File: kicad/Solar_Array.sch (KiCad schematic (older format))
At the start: 23 parts

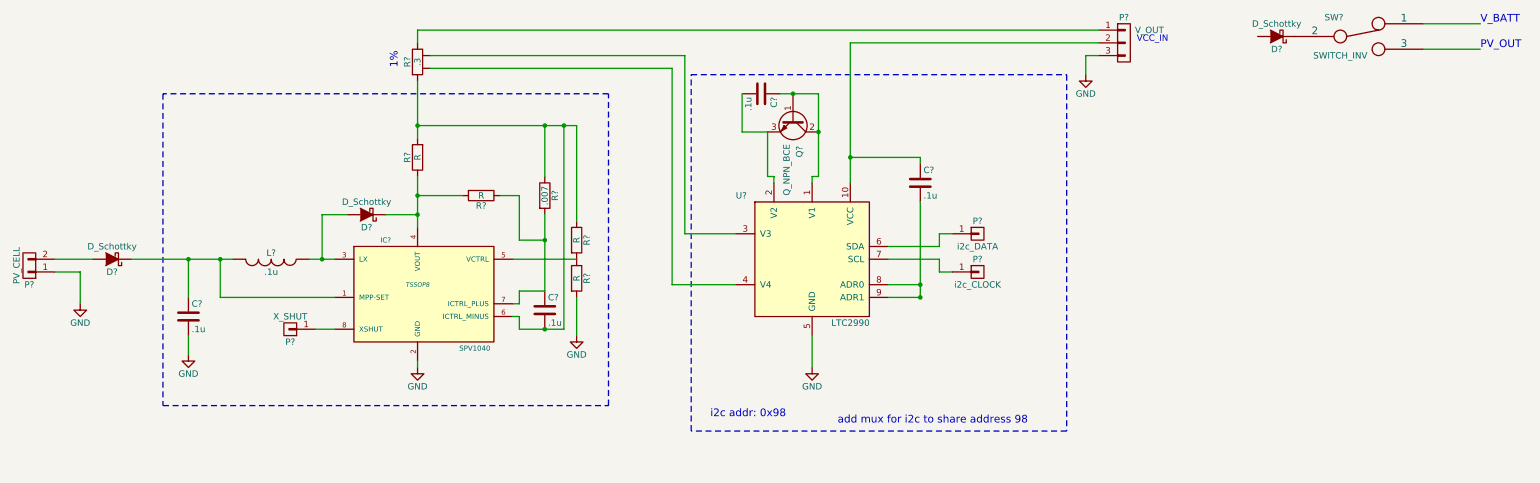
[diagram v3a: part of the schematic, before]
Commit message: Generated Netlist, blocked all I/O to 1x6 pin array.
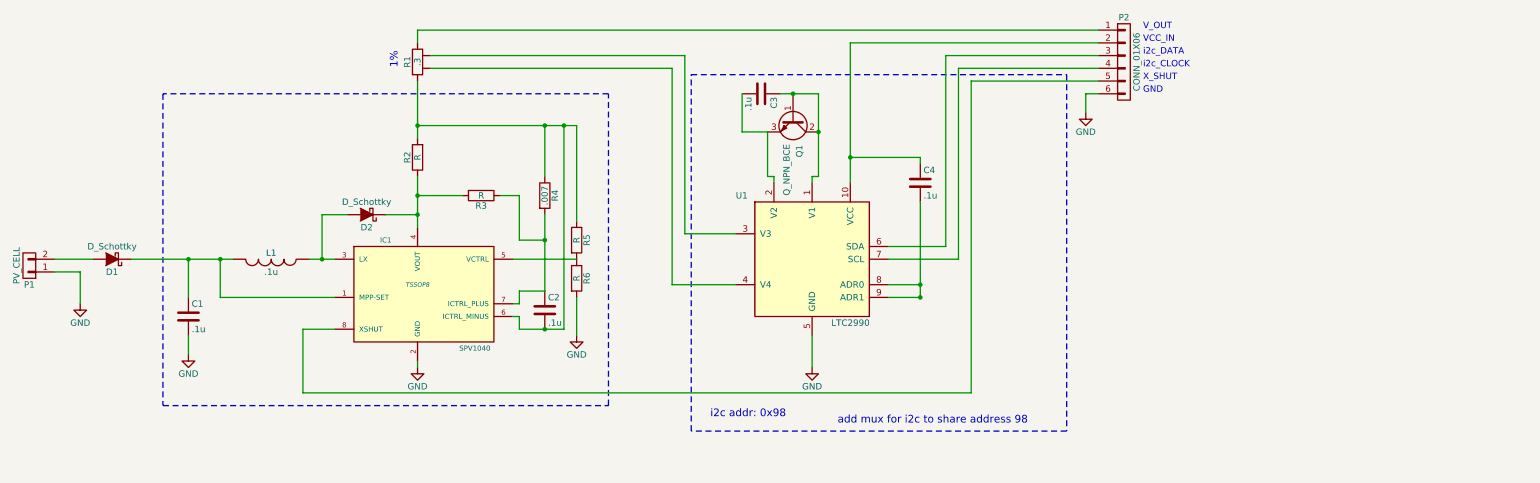
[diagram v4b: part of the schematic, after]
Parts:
- removed D?: D_Schottky, symbol D_Schottky
- removed P?: i2c_CLOCK, symbol CONN_01X01
- removed P?: i2c_DATA, symbol CONN_01X01
- removed P?: X_SHUT, symbol CONN_01X01
- removed P?: V_OUT, symbol CONN_01X03
- removed SW?: SWITCH_INV, symbol SWITCH_INV
- added P2: CONN_01X06, symbol CONN_01X06
- gave numbers to parts that had none: 17
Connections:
- net GND: now also P2.6 (P6)
- net at C4.1, U1.10 (VCC): now also P2.2 (P2)
- net at U1.6 (SDA): now also P2.3 (P3)
- net at U1.7 (SCL): now also P2.4 (P4)
- net at R1.1: now also P2.1 (P1)
- net at IC1.8 (XSHUT): now also P2.5 (P5)
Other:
- note added: "GND"
- note added: "V_OUT"
- note added: "X_SHUT"
- note added: "i2c_CLOCK"
- note added: "i2c_DATA"
- note removed: "PV_OUT"
- note removed: "V_BATT"
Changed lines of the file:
@@
 LIBS:contrib
 LIBS:valves
-LIBS:Launch_Tower_Computer_III-cache
 LIBS:Solar_Array-cache
 EELAYER 25 0
@@
 $EndDescr
 $Comp
-L LTC2990 U?
+L LTC2990 U1
 U 1 1 56A79694
 P 7000 2750
-F 0 "U?" H 6400 3250 50  0000 L CNN
+F 0 "U1" H 6400 3250 50  0000 L CNN
 F 1 "LTC2990" H 7150 2250 50  0000 L CNN
 F 2 "" H 6300 3150 50  0000 C CNN
@@
 $EndComp
 $Comp
-L GND #PWR?
+L GND #PWR01
 U 1 1 56A7969A
 P 7000 3600
-F 0 "#PWR?" H 7000 3350 50  0001 C CNN
+F 0 "#PWR01" H 7000 3350 50  0001 C CNN
 F 1 "GND" H 7000 3450 50  0000 C CNN
 F 2 "" H 7000 3600 60  0000 C CNN
@@
 i2c addr: 0x98
 $Comp
-L R4T R?
+L R4T R1
 U 1 1 56A79735
 P 3900 1200
-F 0 "R?" V 3820 1200 50  0000 C CNN
+F 0 "R1" V 3820 1200 50  0000 C CNN
 F 1 ".3" V 3900 1200 50  0000 C CNN
 F 2 "" V 3830 1200 30  0000 C CNN
@@
 $EndComp
 $Comp
-L Q_NPN_BCE Q?
+L Q_NPN_BCE Q1
 U 1 1 56A7974E
 P 6850 1650
-F 0 "Q?" H 7150 1700 50  0000 R CNN
+F 0 "Q1" H 7150 1700 50  0000 R CNN
 F 1 "Q_NPN_BCE" H 7450 1600 50  0000 R CNN
 F 2 "" H 7050 1750 29  0000 C CNN
@@
 $EndComp
 $Comp
-L C C?
+L C C3
 U 1 1 56A7975A
 P 6600 1450
-F 0 "C?" H 6625 1550 50  0000 L CNN
+F 0 "C3" H 6625 1550 50  0000 L CNN
 F 1 ".1u" H 6625 1350 50  0000 L CNN
 F 2 "" H 6638 1300 30  0000 C CNN
@@
 $EndComp
 $Comp
-L C C?
+L C C4
 U 1 1 56A7DA5A
 P 7850 2150
-F 0 "C?" H 7875 2250 50  0000 L CNN
+F 0 "C4" H 7875 2250 50  0000 L CNN
 F 1 ".1u" H 7875 2050 50  0000 L CNN
 F 2 "" H 7888 2000 30  0000 C CNN
@@
 add mux for i2c to share address 98
 $Comp
-L GND #PWR?
+L GND #PWR02
 U 1 1 56A96BD7
 P 1250 3100
-F 0 "#PWR?" H 1250 2850 50  0001 C CNN
+F 0 "#PWR02" H 1250 2850 50  0001 C CNN
 F 1 "GND" H 1250 2950 50  0000 C CNN
 F 2 "" H 1250 3100 60  0000 C CNN
@@
 $EndComp
 $Comp
-L SPV1040 IC?
+L SPV1040 IC1
 U 1 1 56A9734E
 P 3950 3000
-F 0 "IC?" H 3650 3400 40  0000 C CNN
+F 0 "IC1" H 3650 3400 40  0000 C CNN
 F 1 "SPV1040" H 4350 2550 40  0000 C CNN
 F 2 "TSSOP8" H 3900 3050 35  0000 C CIN
@@
 $EndComp
 $Comp
-L INDUCTOR L?
+L INDUCTOR L1
 U 1 1 56A973BB
 P 2750 2750
-F 0 "L?" V 2700 2750 50  0000 C CNN
+F 0 "L1" V 2700 2750 50  0000 C CNN
 F 1 ".1u" V 2850 2750 50  0000 C CNN
 F 2 "" H 2750 2750 60  0000 C CNN
@@
 $EndComp
 $Comp
-L C C?
+L C C1
 U 1 1 56A97517
 P 2100 3200
-F 0 "C?" H 2125 3300 50  0000 L CNN
+F 0 "C1" H 2125 3300 50  0000 L CNN
 F 1 ".1u" H 2125 3100 50  0000 L CNN
 F 2 "" H 2138 3050 30  0000 C CNN
@@
 $EndComp
 $Comp
-L GND #PWR?
+L GND #PWR03
 U 1 1 56A97606
 P 2100 3500
-F 0 "#PWR?" H 2100 3250 50  0001 C CNN
+F 0 "#PWR03" H 2100 3250 50  0001 C CNN
 F 1 "GND" H 2100 3350 50  0000 C CNN
 F 2 "" H 2100 3500 60  0000 C CNN
@@
 $EndComp
 $Comp
-L C C?
+L C C2
 U 1 1 56A9778A
 P 4900 3150
-F 0 "C?" H 4925 3250 50  0000 L CNN
+F 0 "C2" H 4925 3250 50  0000 L CNN
 F 1 ".1u" H 4925 3050 50  0000 L CNN
 F 2 "" H 4938 3000 30  0000 C CNN
@@
 $EndComp
 $Comp
-L R R?
+L R R5
 U 1 1 56A97A23
 P 5150 2600
-F 0 "R?" V 5230 2600 50  0000 C CNN
+F 0 "R5" V 5230 2600 50  0000 C CNN
 F 1 "R" V 5150 2600 50  0000 C CNN
 F 2 "" V 5080 2600 30  0000 C CNN
@@
 $EndComp
 $Comp
-L R R?
+L R R6
 U 1 1 56A97AAE
 P 5150 2900
-F 0 "R?" V 5230 2900 50  0000 C CNN
+F 0 "R6" V 5230 2900 50  0000 C CNN
 F 1 "R" V 5150 2900 50  0000 C CNN
 F 2 "" V 5080 2900 30  0000 C CNN
@@
 $EndComp
 $Comp
-L GND #PWR?
+L GND #PWR04
 U 1 1 56A97B91
 P 5150 3350
-F 0 "#PWR?" H 5150 3100 50  0001 C CNN
+F 0 "#PWR04" H 5150 3100 50  0001 C CNN
 F 1 "GND" H 5150 3200 50  0000 C CNN
 F 2 "" H 5150 3350 60  0000 C CNN
@@
 $EndComp
 $Comp
-L D_Schottky D?
+L D_Schottky D2
 U 1 1 56A97CB5
 P 3500 2400
-F 0 "D?" H 3500 2500 50  0000 C CNN
+F 0 "D2" H 3500 2500 50  0000 C CNN
 F 1 "D_Schottky" H 3500 2300 50  0000 C CNN
 F 2 "" H 3500 2400 60  0000 C CNN
@@
 $EndComp
 $Comp
-L R R?
+L R R3
 U 1 1 56A9803B
 P 4400 2250
-F 0 "R?" V 4480 2250 50  0000 C CNN
+F 0 "R3" V 4480 2250 50  0000 C CNN
 F 1 "R" V 4400 2250 50  0000 C CNN
 F 2 "" V 4330 2250 30  0000 C CNN
@@
 $EndComp
 $Comp
-L R R?
+L R R2
 U 1 1 56A981E3
 P 3900 1950
-F 0 "R?" V 3980 1950 50  0000 C CNN
+F 0 "R2" V 3980 1950 50  0000 C CNN
 F 1 "R" V 3900 1950 50  0000 C CNN
 F 2 "" V 3830 1950 30  0000 C CNN
@@
 $EndComp
 $Comp
-L R R?
+L R R4
 U 1 1 56A98B14
 P 4900 2250
-F 0 "R?" V 4980 2250 50  0000 C CNN
+F 0 "R4" V 4980 2250 50  0000 C CNN
 F 1 ".007" V 4900 2250 50  0000 C CNN
 F 2 "" V 4830 2250 30  0000 C CNN
@@
 $EndComp
 $Comp
-L GND #PWR?
+L GND #PWR05
 U 1 1 56A99359
 P 3900 3600
-F 0 "#PWR?" H 3900 3350 50  0001 C CNN
+F 0 "#PWR05" H 3900 3350 50  0001 C CNN
 F 1 "GND" H 3900 3450 50  0000 C CNN
 F 2 "" H 3900 3600 60  0000 C CNN
@@
 $EndComp
 $Comp
-L CONN_01X01 P?
-U 1 1 56A9AD7A
-P 8300 2850
-F 0 "P?" H 8300 2950 50  0000 C CNN
-F 1 "i2c_CLOCK" H 8300 2750 50  0000 C CNN
-F 2 "" H 8300 2850 60  0000 C CNN
-F 3 "" H 8300 2850 60  0000 C CNN
-	1    8300 2850
-	1    0    0    -1
-$EndComp
-$Comp
-L CONN_01X01 P?
-U 1 1 56A9B08F
-P 8300 2550
-F 0 "P?" H 8300 2650 50  0000 C CNN
-F 1 "i2c_DATA" H 8300 2450 50  0000 C CNN
-F 2 "" H 8300 2550 60  0000 C CNN
-F 3 "" H 8300 2550 60  0000 C CNN
-	1    8300 2550
-	1    0    0    -1
-$EndComp
-$Comp
-L GND #PWR?
+L GND #PWR06
 U 1 1 56A9DF6A
-P 9150 1300
-F 0 "#PWR?" H 9150 1050 50  0001 C CNN
-F 1 "GND" H 9150 1150 50  0000 C CNN
-F 2 "" H 9150 1300 60  0000 C CNN
-F 3 "" H 9150 1300 60  0000 C CNN
-	1    9150 1300
-	1    0    0    -1
-$EndComp
-$Comp
-L CONN_01X02 P?
+P 9150 1600
+F 0 "#PWR06" H 9150 1350 50  0001 C CNN
+F 1 "GND" H 9150 1450 50  0000 C CNN
+F 2 "" H 9150 1600 60  0000 C CNN
+F 3 "" H 9150 1600 60  0000 C CNN
+	1    9150 1600
+	1    0    0    -1
+$EndComp
+$Comp
+L CONN_01X02 P1
 U 1 1 56A9E16B
 P 850 2800
-F 0 "P?" H 850 2950 50  0000 C CNN
+F 0 "P1" H 850 2950 50  0000 C CNN
 F 1 "PV_CELL" V 950 2800 50  0000 C CNN
 F 2 "" H 850 2800 60  0000 C CNN
@@
 	-1   0    0    1
 $EndComp
-$Comp
-L CONN_01X01 P?
-U 1 1 56AA3494
-P 2900 3300
-F 0 "P?" H 2900 3400 50  0000 C CNN
-F 1 "X_SHUT" H 2900 3200 50  0000 C CNN
-F 2 "" H 2900 3300 60  0000 C CNN
-F 3 "" H 2900 3300 60  0000 C CNN
-	1    2900 3300
-	-1   0    0    1
-$EndComp
-$Comp
-L CONN_01X03 P?
-U 1 1 56AA5ABE
-P 9450 1050
-F 0 "P?" H 9450 1250 50  0000 C CNN
-F 1 "V_OUT" H 9650 1150 50  0000 C CNN
-F 2 "" H 9450 1050 60  0000 C CNN
-F 3 "" H 9450 1050 60  0000 C CNN
-	1    9450 1050
-	1    0    0    -1
-$EndComp
-Text Notes 9550 1050 0    50   ~ 0
+Text Notes 9600 1050 0    50   ~ 0
 VCC_IN
 $Comp
-L D_Schottky D?
+L D_Schottky D1
 U 1 1 56AA70D2
 P 1500 2750
-F 0 "D?" H 1500 2850 50  0000 C CNN
+F 0 "D1" H 1500 2850 50  0000 C CNN
 F 1 "D_Schottky" H 1500 2650 50  0000 C CNN
 F 2 "" H 1500 2750 60  0000 C CNN
@@
 Connection ~ 2100 2750
 Wire Wire Line
-	7600 2750 8000 2750
-Wire Wire Line
-	8000 2750 8000 2850
-Wire Wire Line
-	8000 2850 8100 2850
-Wire Wire Line
-	7600 2650 8000 2650
-Wire Wire Line
-	8000 2650 8000 2550
-Wire Wire Line
-	8000 2550 8100 2550
+	7600 2750 8150 2750
+Wire Wire Line
+	7600 2650 8050 2650
 Wire Wire Line
 	4700 2250 4700 2600
@@
 	3900 950  3900 1050
 Wire Wire Line
-	3100 3300 3250 3300
+	3000 3300 3250 3300
 Wire Wire Line
 	3900 1700 5150 1700
@@
 	3900 2250 4250 2250
 Wire Wire Line
-	9150 1150 9250 1150
-Wire Wire Line
-	9150 1150 9150 1300
+	8050 1150 9250 1150
 Wire Wire Line
 	7300 1050 9250 1050
@@
 Wire Wire Line
 	1650 2750 2450 2750
-$Comp
-L D_Schottky D?
-U 1 1 56AC3033
-P 10650 1000
-F 0 "D?" H 10650 1100 50  0000 C CNN
-F 1 "D_Schottky" H 10650 900 50  0000 C CNN
-F 2 "" H 10650 1000 60  0000 C CNN
-F 3 "" H 10650 1000 60  0000 C CNN
-	1    10650 1000
-	-1   0    0    1
-$EndComp
-$Comp
-L SWITCH_INV SW?
-U 1 1 56AC30B8
-P 11300 1000
-F 0 "SW?" H 11100 1150 50  0000 C CNN
-F 1 "SWITCH_INV" H 11150 850 50  0000 C CNN
-F 2 "" H 11300 1000 60  0000 C CNN
-F 3 "" H 11300 1000 60  0000 C CNN
-	1    11300 1000
-	1    0    0    -1
-$EndComp
-Wire Wire Line
-	11800 900  12250 900
-Wire Wire Line
-	11800 1100 12250 1100
-Text Notes 12250 900  0    60   ~ 0
-V_BATT
-Text Notes 12250 1100 0    60   ~ 0
-PV_OUT
+Wire Wire Line
+	8250 1350 9250 1350
+Wire Wire Line
+	8050 2650 8050 1150
+Wire Wire Line
+	8150 2750 8150 1250
+Wire Wire Line
+	8150 1250 9250 1250
+$Comp
+L CONN_01X06 P2
+U 1 1 56B283C9
+P 9450 1200
+F 0 "P2" H 9450 1550 50  0000 C CNN
+F 1 "CONN_01X06" V 9550 1200 50  0000 C CNN
+F 2 "" H 9450 1200 60  0000 C CNN
+F 3 "" H 9450 1200 60  0000 C CNN
+	1    9450 1200
+	1    0    0    -1
+$EndComp
+Wire Wire Line
+	9250 1450 9150 1450
+Wire Wire Line
+	9150 1450 9150 1600
+Wire Wire Line
+	8250 1350 8250 3800
+Wire Wire Line
+	8250 3800 3000 3800
+Wire Wire Line
+	3000 3800 3000 3300
+Text Notes 9600 950  0    50   ~ 0
+V_OUT
+Text Notes 9600 1150 0    50   ~ 0
+i2c_DATA
+Text Notes 9600 1250 0    50   ~ 0
+i2c_CLOCK
+Text Notes 9600 1350 0    50   ~ 0
+X_SHUT
+Text Notes 9600 1450 0    50   ~ 0
+GND
 $EndSCHEMATC

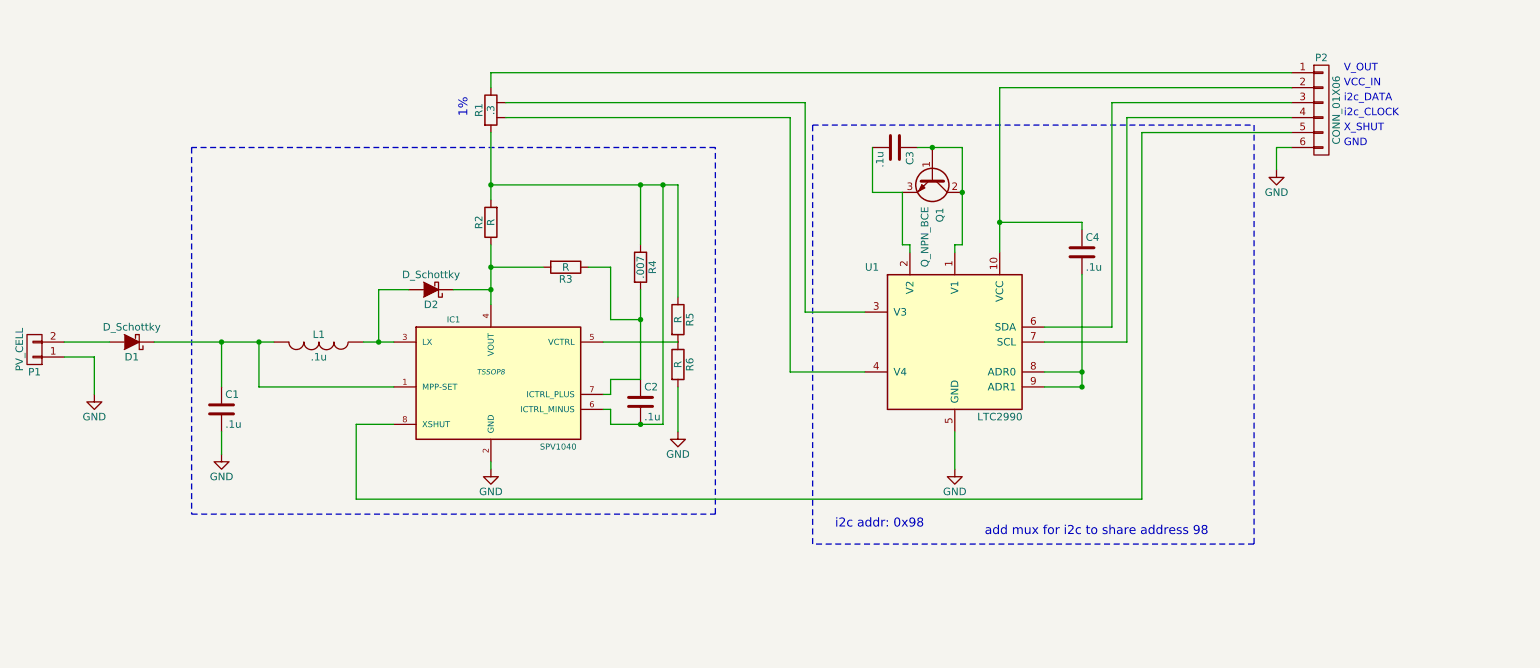
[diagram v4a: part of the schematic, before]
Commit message: Removed input shotkey diode, adde design notes, readdressed ltc2990.
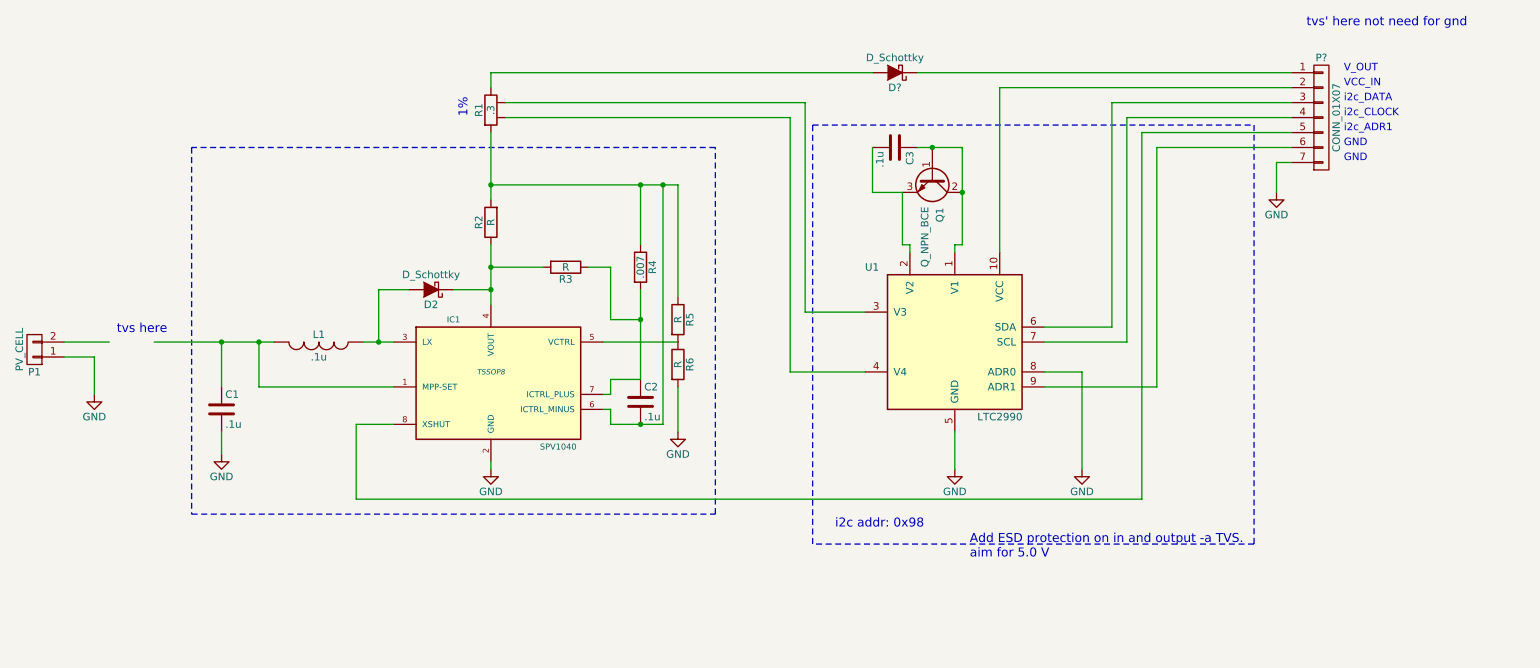
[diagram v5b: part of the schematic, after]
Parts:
- removed C4: .1u, symbol C
- removed D1: D_Schottky, symbol D_Schottky
- removed P2: CONN_01X06, symbol CONN_01X06
- added D?: D_Schottky, symbol D_Schottky
- added P?: CONN_01X07, symbol CONN_01X07
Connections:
- net GND: now also U1.8 (ADR0), P?.7 (P7)
- net at U1.10 (VCC): now also P?.2 (P2)
- net at U1.6 (SDA): now also P?.3 (P3)
- net at U1.7 (SCL): now also P?.4 (P4)
- net at U1.9 (ADR1): now also P?.6 (P6); no longer U1.8 (ADR0)
- net at R1.1: now also D?.2 (A)
- net at IC1.8 (XSHUT): now also P?.5 (P5)
- new net: D?.1 (K), P?.1 (P1)
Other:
- note added: "Add ESD protection on in and output -a TVS.\naim for 5.0 V"
- note added: "i2c_ADR1"
- note added: "tvs here"
- note added: "tvs' here not need for gnd"
- note removed: "X_SHUT"
- note removed: "add mux for i2c to share address 98"
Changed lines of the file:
@@
 LIBS:contrib
 LIBS:valves
+LIBS:Launch_Tower_Computer_III-cache
 LIBS:Solar_Array-cache
 EELAYER 25 0
@@
 	0    1    1    0
 $EndComp
-$Comp
-L C C4
-U 1 1 56A7DA5A
-P 7850 2150
-F 0 "C4" H 7875 2250 50  0000 L CNN
-F 1 ".1u" H 7875 2050 50  0000 L CNN
-F 2 "" H 7888 2000 30  0000 C CNN
-F 3 "" H 7850 2150 60  0000 C CNN
-	1    7850 2150
-	1    0    0    -1
-$EndComp
 Text Notes 1200 9750 0    60   ~ 0
 ToDo:\n***Select component values\n***Design more robust automatic shutdown\n***Add mux for i2c\n***Low voltage warning to payload for save and reboot.\n***3.3v for uC (10 ma each uC)\n***PA need 20V
 Text Notes 3750 1250 1    60   ~ 0
 1%
-Text Notes 7200 4050 0    60   ~ 0
-add mux for i2c to share address 98
 $Comp
 L GND #PWR02
@@
 L GND #PWR06
 U 1 1 56A9DF6A
-P 9150 1600
-F 0 "#PWR06" H 9150 1350 50  0001 C CNN
-F 1 "GND" H 9150 1450 50  0000 C CNN
-F 2 "" H 9150 1600 60  0000 C CNN
-F 3 "" H 9150 1600 60  0000 C CNN
-	1    9150 1600
+P 9150 1750
+F 0 "#PWR06" H 9150 1500 50  0001 C CNN
+F 1 "GND" H 9150 1600 50  0000 C CNN
+F 2 "" H 9150 1750 60  0000 C CNN
+F 3 "" H 9150 1750 60  0000 C CNN
+	1    9150 1750
 	1    0    0    -1
 $EndComp
@@
 Text Notes 9600 1050 0    50   ~ 0
 VCC_IN
-$Comp
-L D_Schottky D1
-U 1 1 56AA70D2
-P 1500 2750
-F 0 "D1" H 1500 2850 50  0000 C CNN
-F 1 "D_Schottky" H 1500 2650 50  0000 C CNN
-F 2 "" H 1500 2750 60  0000 C CNN
-F 3 "" H 1500 2750 60  0000 C CNN
-	1    1500 2750
-	-1   0    0    1
-$EndComp
 Text Notes 3900 9500 0    60   ~ 0
 Notes:\n***3.3v for uC (10 ma each uC)\n***PA need 20V\n***Test BQ3060
@@
 	7600 2950 7850 2950
 Wire Wire Line
-	7850 3050 7600 3050
-Connection ~ 7850 3050
-Connection ~ 7850 2950
-Wire Wire Line
-	7850 2000 7850 1950
-Wire Wire Line
-	7850 1950 7300 1950
-Connection ~ 7300 1950
+	7600 3050 8350 3050
 Wire Notes Line
 	9000 1300 9000 4100
@@
 Wire Notes Line
 	6050 4100 6050 1300
-Wire Wire Line
-	7850 2300 7850 3050
 Wire Wire Line
 	5900 2950 6400 2950
@@
 	6000 1150 4000 1150
 Wire Wire Line
-	3900 950  9250 950
-Wire Wire Line
 	3900 950  3900 1050
 Wire Wire Line
@@
 Wire Wire Line
 	8150 1250 9250 1250
-$Comp
-L CONN_01X06 P2
-U 1 1 56B283C9
-P 9450 1200
-F 0 "P2" H 9450 1550 50  0000 C CNN
-F 1 "CONN_01X06" V 9550 1200 50  0000 C CNN
-F 2 "" H 9450 1200 60  0000 C CNN
-F 3 "" H 9450 1200 60  0000 C CNN
-	1    9450 1200
-	1    0    0    -1
-$EndComp
-Wire Wire Line
-	9250 1450 9150 1450
-Wire Wire Line
-	9150 1450 9150 1600
 Wire Wire Line
 	8250 1350 8250 3800
@@
 i2c_CLOCK
 Text Notes 9600 1350 0    50   ~ 0
-X_SHUT
+i2c_ADR1
+Text Notes 9600 1550 0    50   ~ 0
+GND
+$Comp
+L D_Schottky D?
+U 1 1 56BAC557
+P 6600 950
+F 0 "D?" H 6600 1050 50  0000 C CNN
+F 1 "D_Schottky" H 6600 850 50  0000 C CNN
+F 2 "" H 6600 950 60  0000 C CNN
+F 3 "" H 6600 950 60  0000 C CNN
+	1    6600 950
+	-1   0    0    1
+$EndComp
+Wire Wire Line
+	3900 950  6450 950
+Wire Wire Line
+	6750 950  9250 950
+Text Notes 7100 4200 0    60   ~ 0
+Add ESD protection on in and output -a TVS.\naim for 5.0 V
+Text Notes 1400 2700 0    60   ~ 0
+tvs here
+Text Notes 9350 650  0    60   ~ 0
+tvs' here not need for gnd
+$Comp
+L GND #PWR?
+U 1 1 56BAE8DD
+P 7850 3600
+F 0 "#PWR?" H 7850 3350 50  0001 C CNN
+F 1 "GND" H 7850 3450 50  0000 C CNN
+F 2 "" H 7850 3600 50  0000 C CNN
+F 3 "" H 7850 3600 50  0000 C CNN
+	1    7850 3600
+	1    0    0    -1
+$EndComp
+Wire Wire Line
+	7850 2950 7850 3600
+Wire Wire Line
+	8350 3050 8350 1450
+Wire Wire Line
+	8350 1450 9250 1450
+$Comp
+L CONN_01X07 P?
+U 1 1 56BAEA85
+P 9450 1250
+F 0 "P?" H 9450 1650 50  0000 C CNN
+F 1 "CONN_01X07" V 9550 1250 50  0000 C CNN
+F 2 "" H 9450 1250 50  0000 C CNN
+F 3 "" H 9450 1250 50  0000 C CNN
+	1    9450 1250
+	1    0    0    -1
+$EndComp
+Wire Wire Line
+	9250 1550 9150 1550
+Wire Wire Line
+	9150 1550 9150 1750
 Text Notes 9600 1450 0    50   ~ 0
 GND
